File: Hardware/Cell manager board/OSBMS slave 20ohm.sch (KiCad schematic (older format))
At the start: 72 parts, among them P1 CONN_01X07, P2 EXT-TMP, P3 CONN_01X09, P4 CONN_01X09, Q1 BSS138, Q2 BSS138, Q3 BSS138, Q4 BSS138, Q5 BSS138, Q6 BSS138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

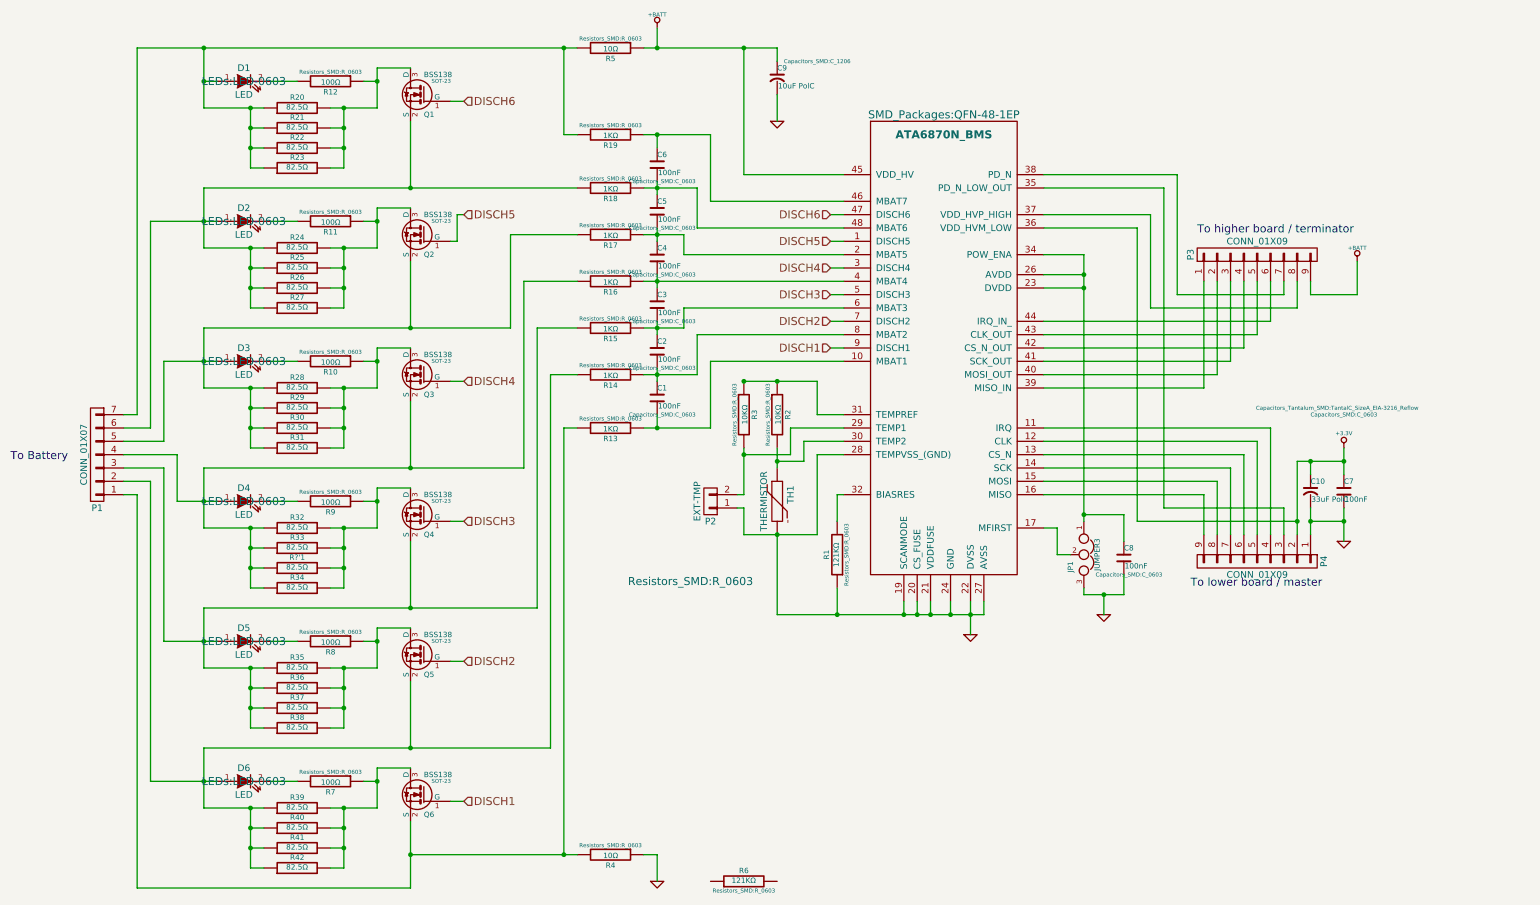
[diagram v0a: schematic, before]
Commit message: changed design to use better resistors
revamped design to use more commonly avalable resistors and resistor
packs that should protect the mosfet gates in the event of a voltage
spike etc.  also improved thermal design. some thermal stitching still
has to be done but is quite tedious
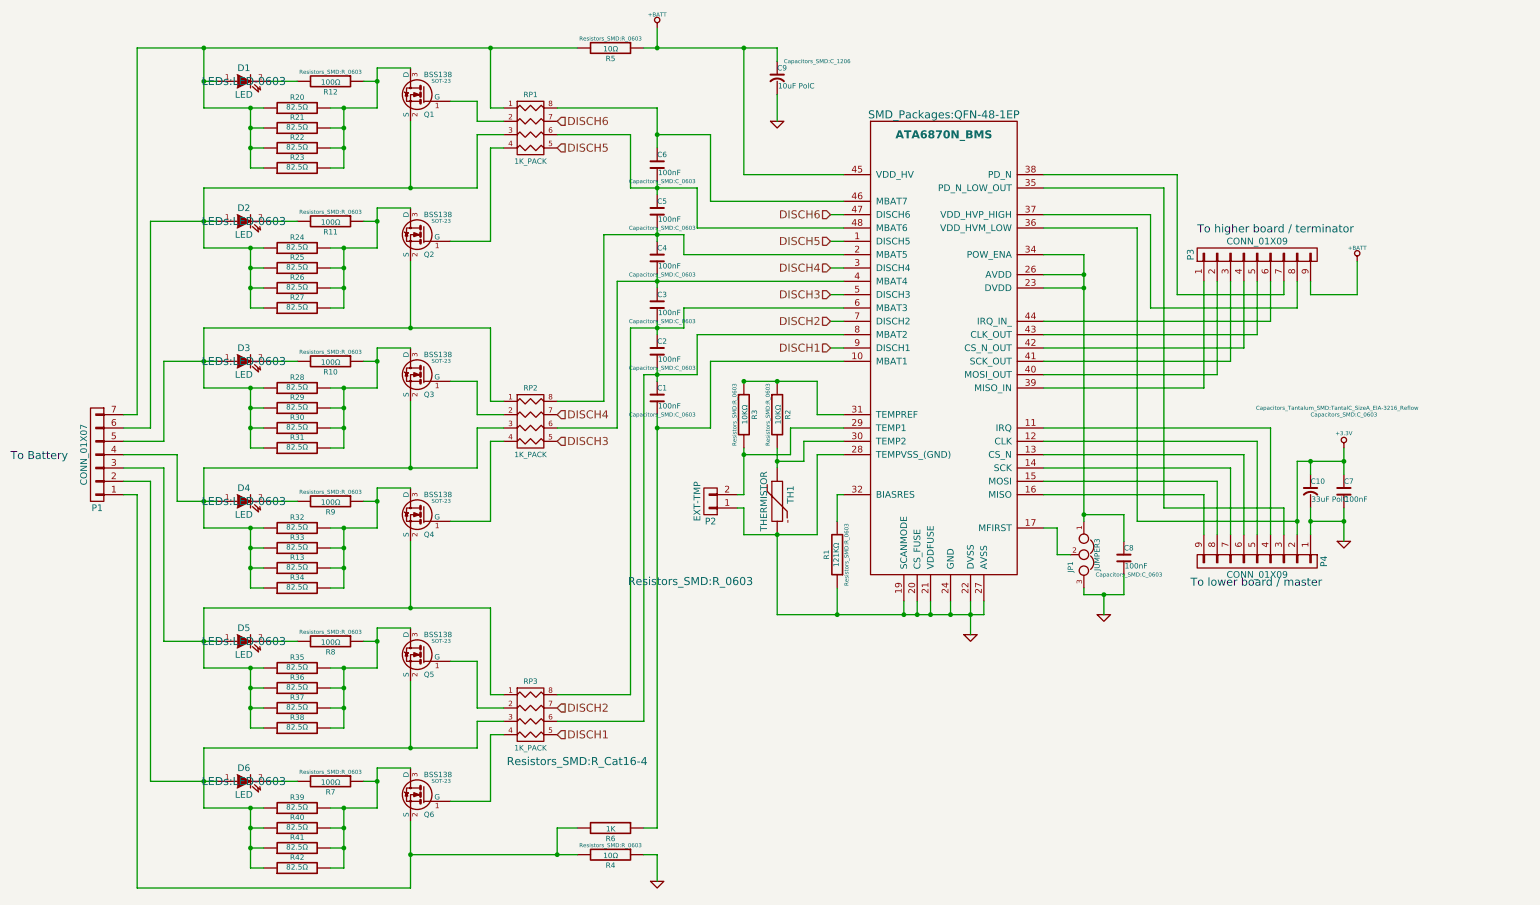
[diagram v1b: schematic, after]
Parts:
- removed R13, R14, R15, R16, R17, R18, R19: 1KΩ, Resistors_SMD:R_0603, symbol R
- added RP1, RP2, RP3: 1K_PACK, Resistors_SMD:R_Cat16-4, symbol R_PACK4
- R6: value 121KΩ -> 1K; footprint Resistors_SMD:R_0603 -> (none)
- renumbered R?'1 to R13
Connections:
- net DISCH1: now also RP3.5 (R4); no longer Q6.1 (G)
- net DISCH2: now also RP3.7 (R2); no longer Q5.1 (G)
- net DISCH3: now also RP2.5 (R4); no longer Q4.1 (G)
- net DISCH4: now also RP2.7 (R2); no longer Q3.1 (G)
- net DISCH5: now also RP1.5 (R4); no longer Q2.1 (G)
- net DISCH6: now also RP1.7 (R2); no longer Q1.1 (G)
- net at D2.1 (A), P1.6 (P6), Q1.2 (S)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: now also RP1.3 (P3)
- net at C1.2, U1.10 (MBAT1): now also R6.1
- net at C4.1, C5.2, U1.2 (MBAT5): now also RP2.8 (R1)
- net at C3.1, C4.2, U1.4 (MBAT4): now also RP2.6 (R3)
- net at C6.1, U1.46 (MBAT7): now also RP1.8 (R1)
- net at C5.1, C6.2, U1.48 (MBAT6): now also RP1.6 (R3)
- net at C2.1, C3.2, U1.6 (MBAT3): now also RP3.8 (R1)
- net at C1.1, C2.2, U1.8 (MBAT2): now also RP3.6 (R3)
- net at D1.1 (A), P1.7 (P7), R20.1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: now also RP1.1 (P1)
- net at P1.1 (P1), Q6.2 (S), R4.2: now also R6.2
- net at D6.1 (A), P1.2 (P2), Q5.2 (S)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: now also RP3.3 (P3)
- net at D5.1 (A), P1.3 (P3), Q4.2 (S)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: now also RP3.1 (P1)
- net at D4.1 (A), P1.4 (P4), Q3.2 (S)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: now also RP2.3 (P3)
- net at D3.1 (A), P1.5 (P5), Q2.2 (S)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: now also RP2.1 (P1)
- new net: Q1.1 (G), RP1.2 (P2)
- new net: Q2.1 (G), RP1.4 (P4)
- new net: Q3.1 (G), RP2.2 (P2)
- new net: Q6.1 (G), RP3.4 (P4)
- new net: Q4.1 (G), RP2.4 (P4)
- new net: Q5.1 (G), RP3.2 (P2)

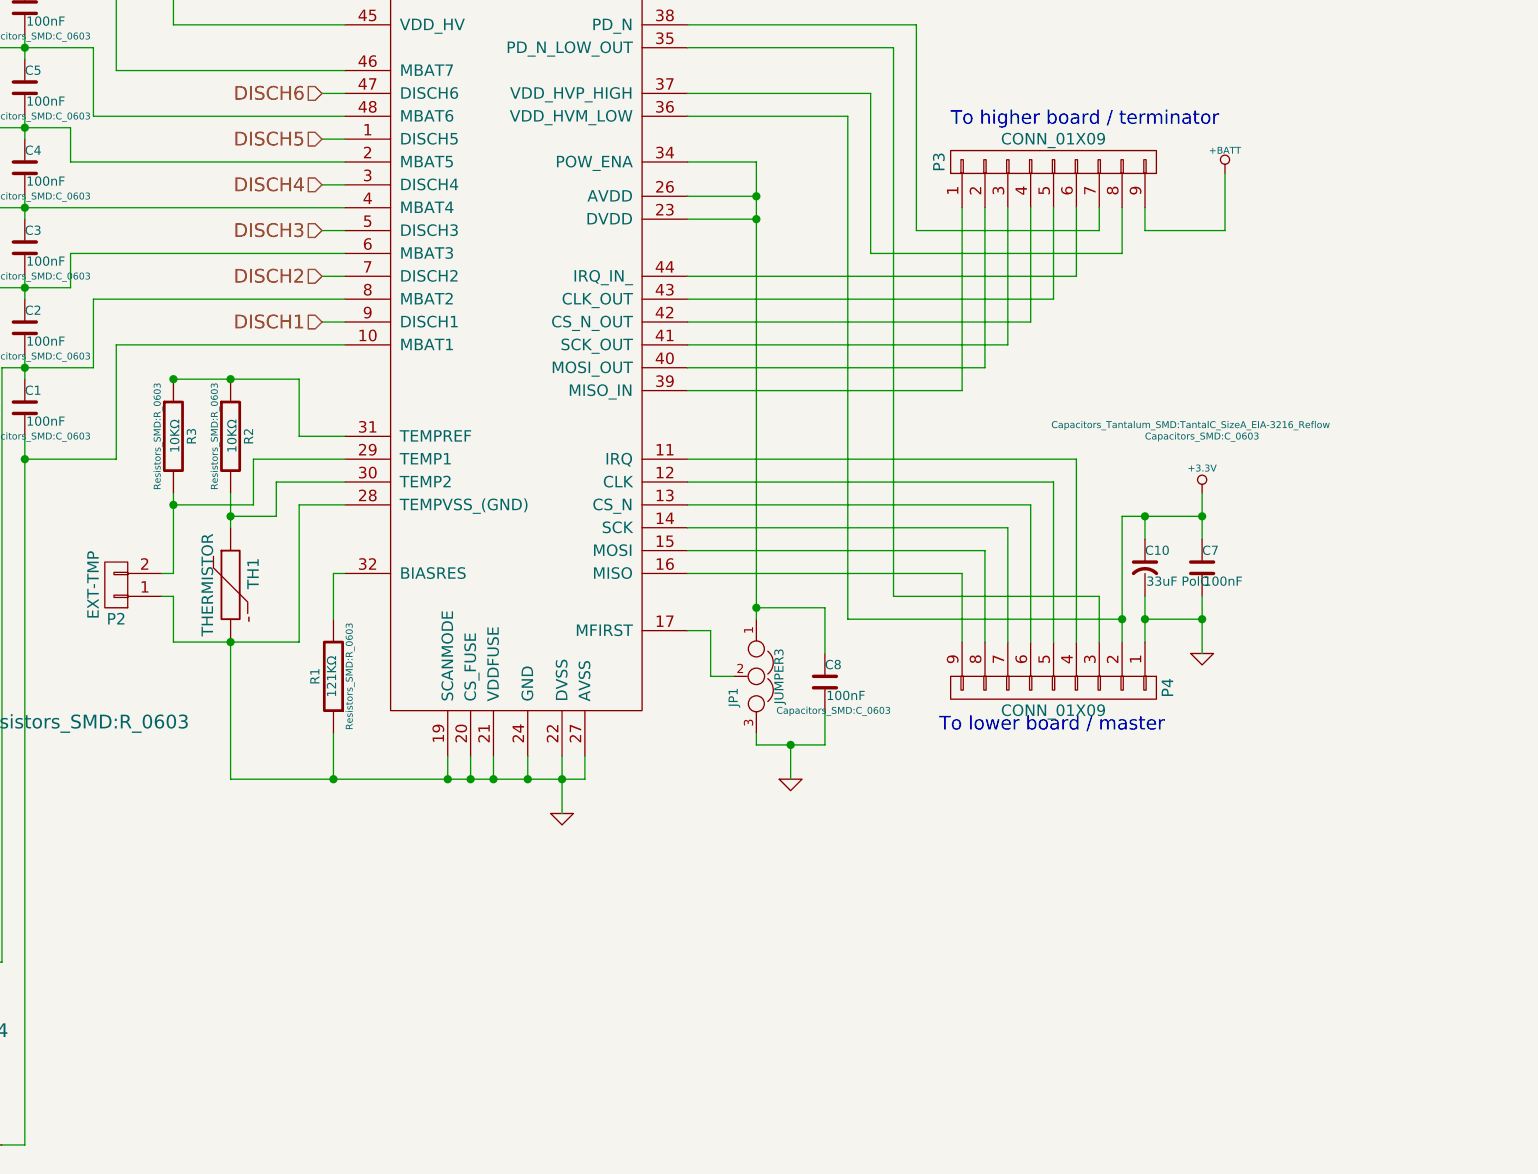
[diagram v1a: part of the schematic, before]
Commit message: finished resistor change and via stiching
finished resistor change and via stiching. board is now functional (at
least I hope) the last thing to do is tidy up the silkscreen and
soldermask
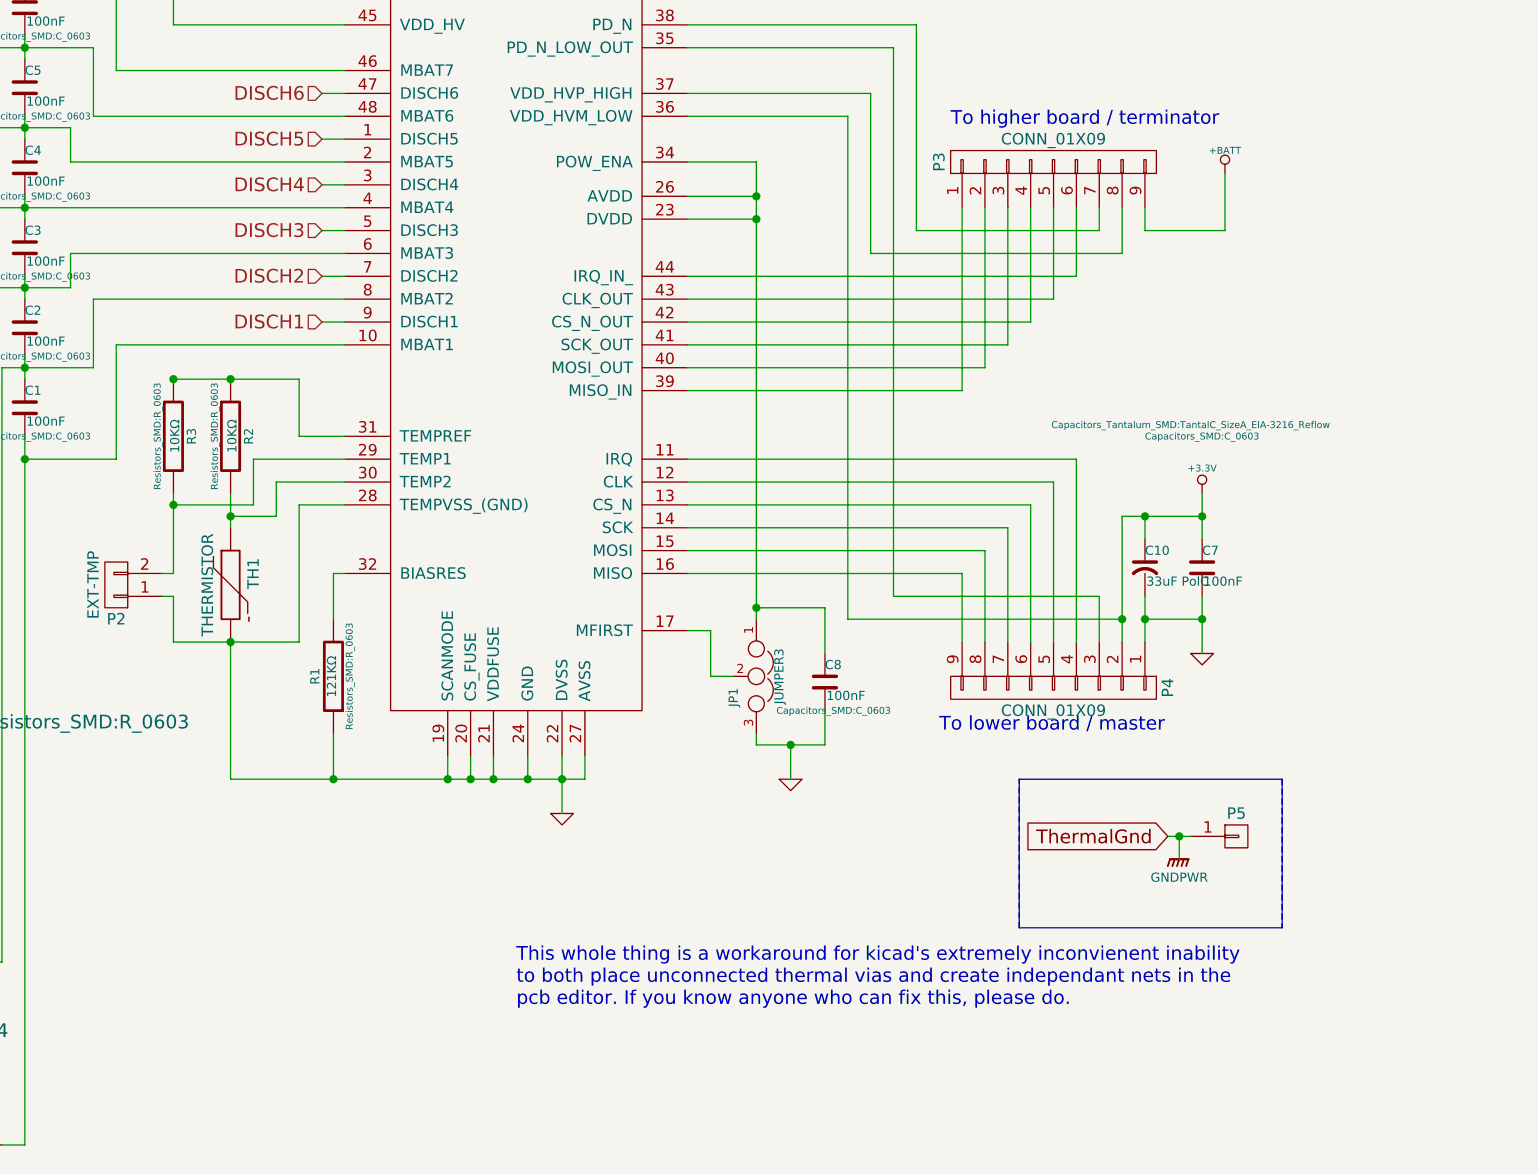
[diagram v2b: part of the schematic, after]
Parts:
- added P5: CONN_01X01, SMD_Packages:1Pin, symbol CONN_01X01
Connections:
- new net GNDPWR: P5.1 (P1)
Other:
- note added: "This whole thing is a workaround for kicad's extremely inconvienent inability\nto both place unconnected thermal vias and create independant nets in the \npcb editor. If you know anyone who can fix this, please do."
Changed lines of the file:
@@
 $EndComp
 $Comp
-L +BATT #PWR01
+L +BATT #PWR1
 U 1 1 54188DB8
 P 5400 1100
-F 0 "#PWR01" H 5400 1050 20  0001 C CNN
+F 0 "#PWR1" H 5400 1050 20  0001 C CNN
 F 1 "+BATT" H 5400 1200 30  0000 C CNN
 F 2 "" H 5400 1100 60  0000 C CNN
@@
 $EndComp
 $Comp
-L GND #PWR02
+L GND #PWR7
 U 1 1 54188E78
 P 7750 5650
-F 0 "#PWR02" H 7750 5650 30  0001 C CNN
+F 0 "#PWR7" H 7750 5650 30  0001 C CNN
 F 1 "GND" H 7750 5580 30  0001 C CNN
 F 2 "" H 7750 5650 60  0000 C CNN
@@
 To Battery
 $Comp
-L GND #PWR03
+L GND #PWR9
 U 1 1 54237CBF
 P 5400 7500
-F 0 "#PWR03" H 5400 7500 30  0001 C CNN
+F 0 "#PWR9" H 5400 7500 30  0001 C CNN
 F 1 "GND" H 5400 7430 30  0001 C CNN
 F 2 "" H 5400 7500 60  0000 C CNN
@@
 $EndComp
 $Comp
-L GND #PWR04
+L GND #PWR2
 U 1 1 54268087
 P 6300 1800
-F 0 "#PWR04" H 6300 1800 30  0001 C CNN
+F 0 "#PWR2" H 6300 1800 30  0001 C CNN
 F 1 "GND" H 6300 1730 30  0001 C CNN
 F 2 "" H 6300 1800 60  0000 C CNN
@@
 $EndComp
 $Comp
-L GND #PWR05
+L GND #PWR5
 U 1 1 54255D02
 P 10550 4950
-F 0 "#PWR05" H 10550 4950 30  0001 C CNN
+F 0 "#PWR5" H 10550 4950 30  0001 C CNN
 F 1 "GND" H 10550 4880 30  0001 C CNN
 F 2 "" H 10550 4950 60  0000 C CNN
@@
 $EndComp
 $Comp
-L +BATT #PWR06
+L +BATT #PWR3
 U 1 1 54257090
 P 10650 2850
-F 0 "#PWR06" H 10650 2800 20  0001 C CNN
+F 0 "#PWR3" H 10650 2800 20  0001 C CNN
 F 1 "+BATT" H 10650 2950 30  0000 C CNN
 F 2 "" H 10650 2850 60  0000 C CNN
@@
 $EndComp
 $Comp
-L GND #PWR07
+L GND #PWR6
 U 1 1 5425E157
 P 8750 5500
-F 0 "#PWR07" H 8750 5500 30  0001 C CNN
+F 0 "#PWR6" H 8750 5500 30  0001 C CNN
 F 1 "GND" H 8750 5430 30  0001 C CNN
 F 2 "" H 8750 5500 60  0000 C CNN
@@
 $EndComp
 $Comp
-L +3.3V #PWR08
+L +3.3V #PWR4
 U 1 1 54266B58
 P 10550 4250
-F 0 "#PWR08" H 10550 4210 30  0001 C CNN
+F 0 "#PWR4" H 10550 4210 30  0001 C CNN
 F 1 "+3.3V" H 10550 4360 30  0000 C CNN
 F 2 "" H 10550 4250 60  0000 C CNN
@@
 	6050 4700 6000 4700
 Wire Wire Line
-	6000 4600 6050 4600
-Wire Wire Line
-	6050 4600 6050 4250
+	6050 4600 6000 4600
+Wire Wire Line
+	6050 4250 6050 4600
 Wire Wire Line
 	6050 3750 6600 3750
@@
 Connection ~ 6300 3750
 Wire Wire Line
-	6300 4400 6300 4250
+	6300 4250 6300 4400
 Connection ~ 6050 4300
 Wire Wire Line
@@
 	8400 5050 8500 5050
 Wire Wire Line
-	8600 4800 8600 2800
+	8600 2800 8600 4800
 Wire Wire Line
 	8600 2800 8300 2800
@@
 	0    1    1    0
 $EndComp
+$Comp
+L GNDPWR #PWR8
+U 1 1 543C52AA
+P 10450 5850
+F 0 "#PWR8" H 10450 5900 40  0001 C CNN
+F 1 "GNDPWR" H 10450 5770 40  0000 C CNN
+F 2 "" H 10450 5850 60  0000 C CNN
+F 3 "" H 10450 5850 60  0000 C CNN
+	1    10450 5850
+	1    0    0    -1
+$EndComp
+Text GLabel 10400 5750 0    60   Input ~ 0
+ThermalGnd
+Wire Notes Line
+	10900 5500 10900 6150
+Wire Notes Line
+	9750 6150 9750 5500
+Text Notes 7550 6500 0    60   ~ 0
+This whole thing is a workaround for kicad's extremely inconvienent inability\nto both place unconnected thermal vias and create independant nets in the \npcb editor. If you know anyone who can fix this, please do.
+$Comp
+L CONN_01X01 P5
+U 1 1 543D6344
+P 10700 5750
+F 0 "P5" H 10700 5850 50  0000 C CNN
+F 1 "CONN_01X01" V 10800 5750 50  0001 C CNN
+F 2 "SMD_Packages:1Pin" H 10700 5750 60  0001 C CNN
+F 3 "" H 10700 5750 60  0000 C CNN
+	1    10700 5750
+	1    0    0    -1
+$EndComp
+Wire Wire Line
+	10400 5750 10500 5750
+Wire Wire Line
+	10450 5750 10450 5850
+Connection ~ 10450 5750
+Wire Bus Line
+	10900 5500 9750 5500
+Wire Bus Line
+	9750 6150 10900 6150
+Wire Bus Line
+	10900 6150 10900 5500
+Wire Bus Line
+	9750 5500 9750 6150
 $EndSCHEMATC
